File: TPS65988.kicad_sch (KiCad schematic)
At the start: 50 parts, among them J5 USB_C_Receptacle, J6 USB_C_Receptacle, J7 Conn_01x05, U13 TPD6S300A, U14 TPS65988, U15 TPD6S300A

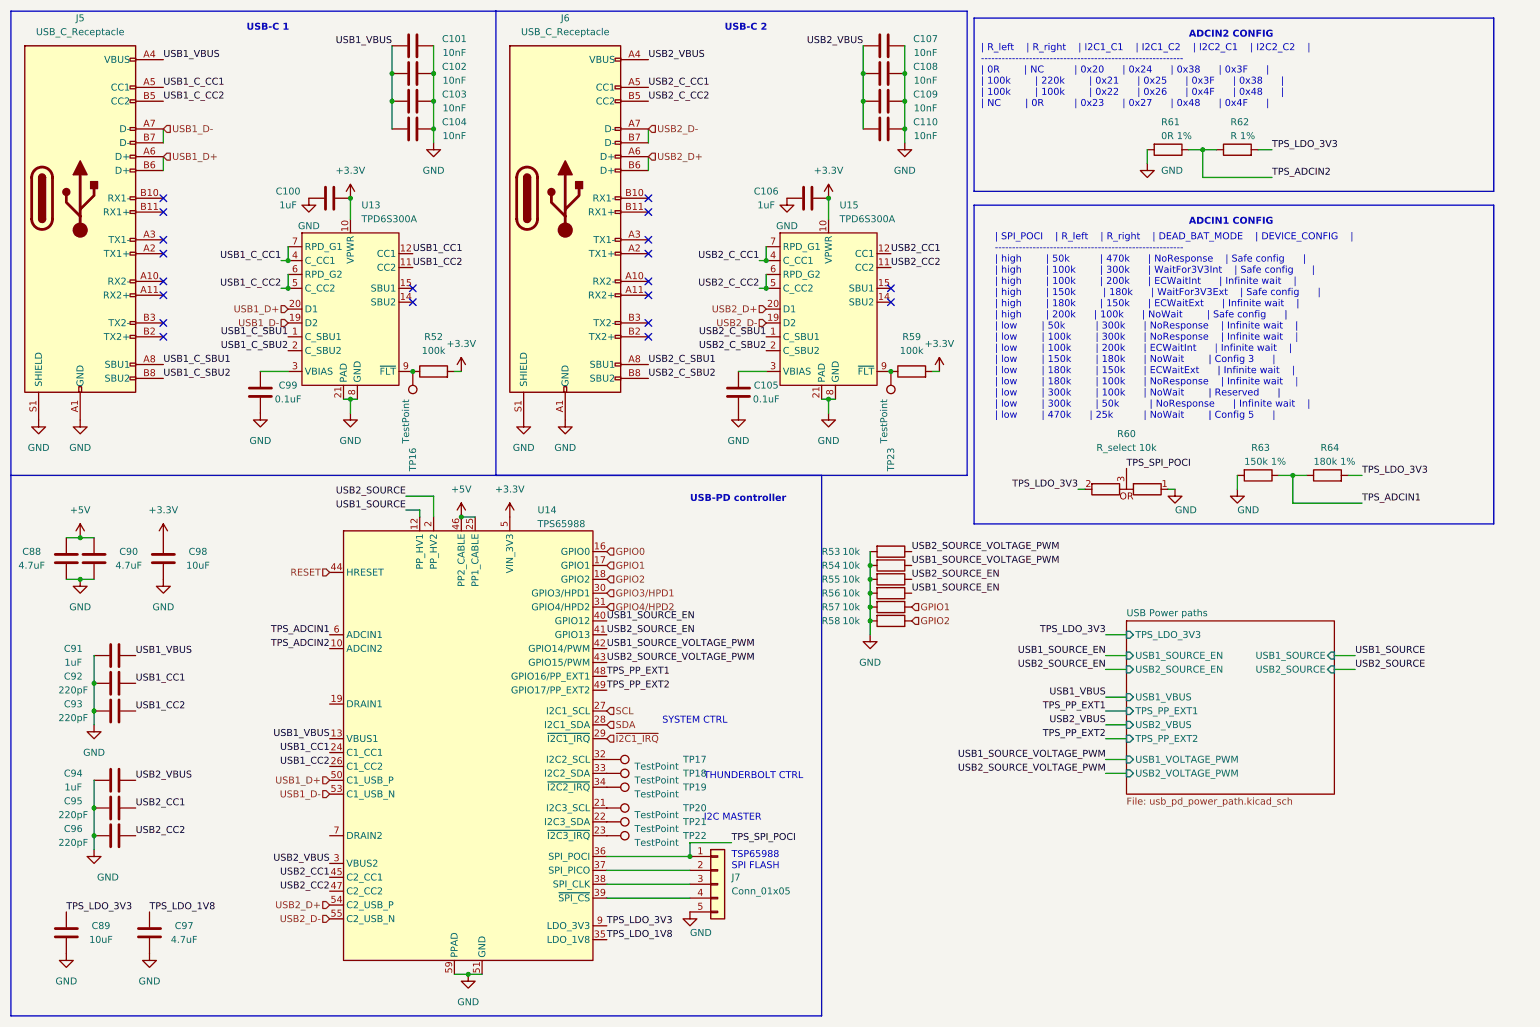
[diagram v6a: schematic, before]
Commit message: copied own LED footprint, modified silkscreen, minor visual changes in schematics
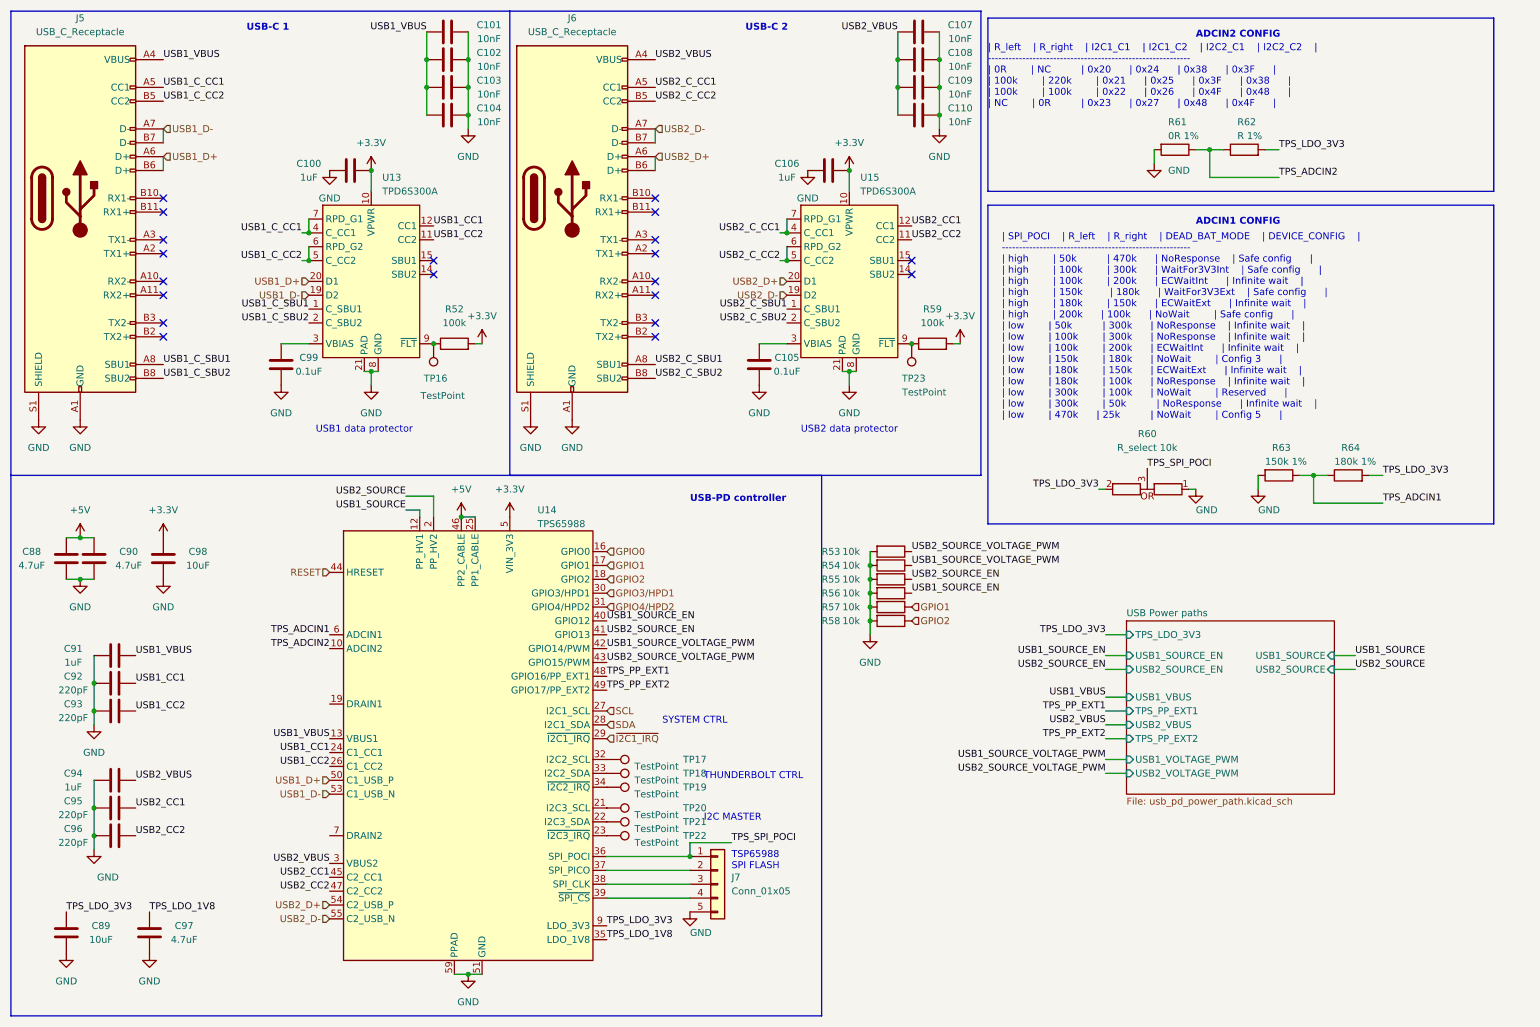
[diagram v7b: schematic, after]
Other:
- note added: "USB1 data protector"
- note added: "USB2 data protector"
- moved on the sheet: C100, C101, C102, C103, C104, C105, C106, C107, C108, C109, C110, C99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
